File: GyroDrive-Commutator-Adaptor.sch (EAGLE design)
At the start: 26 parts, among them U1 HALL, U2 PCA9517, U3 5V, U4 2.5V, U5 INA2141U, U6 INA2141U, U7 INA2141U, X1 NORCOMP-DB25-SMD-MALE

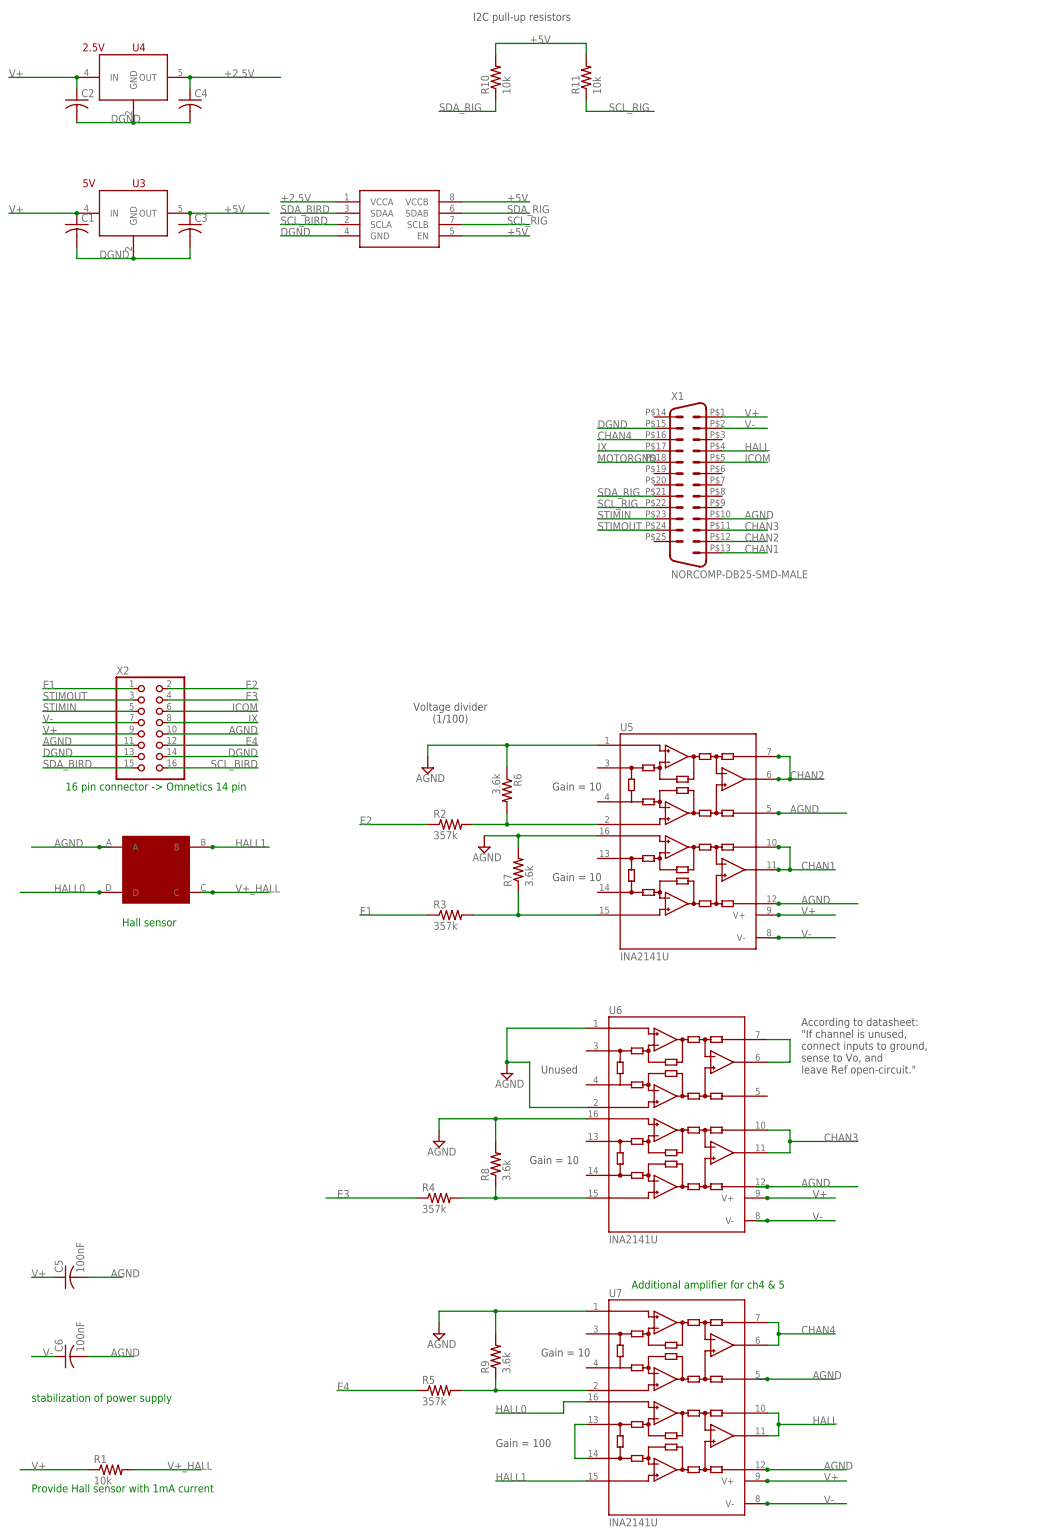
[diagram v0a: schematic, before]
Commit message: Removed instrumentation amplifiers for electrodes
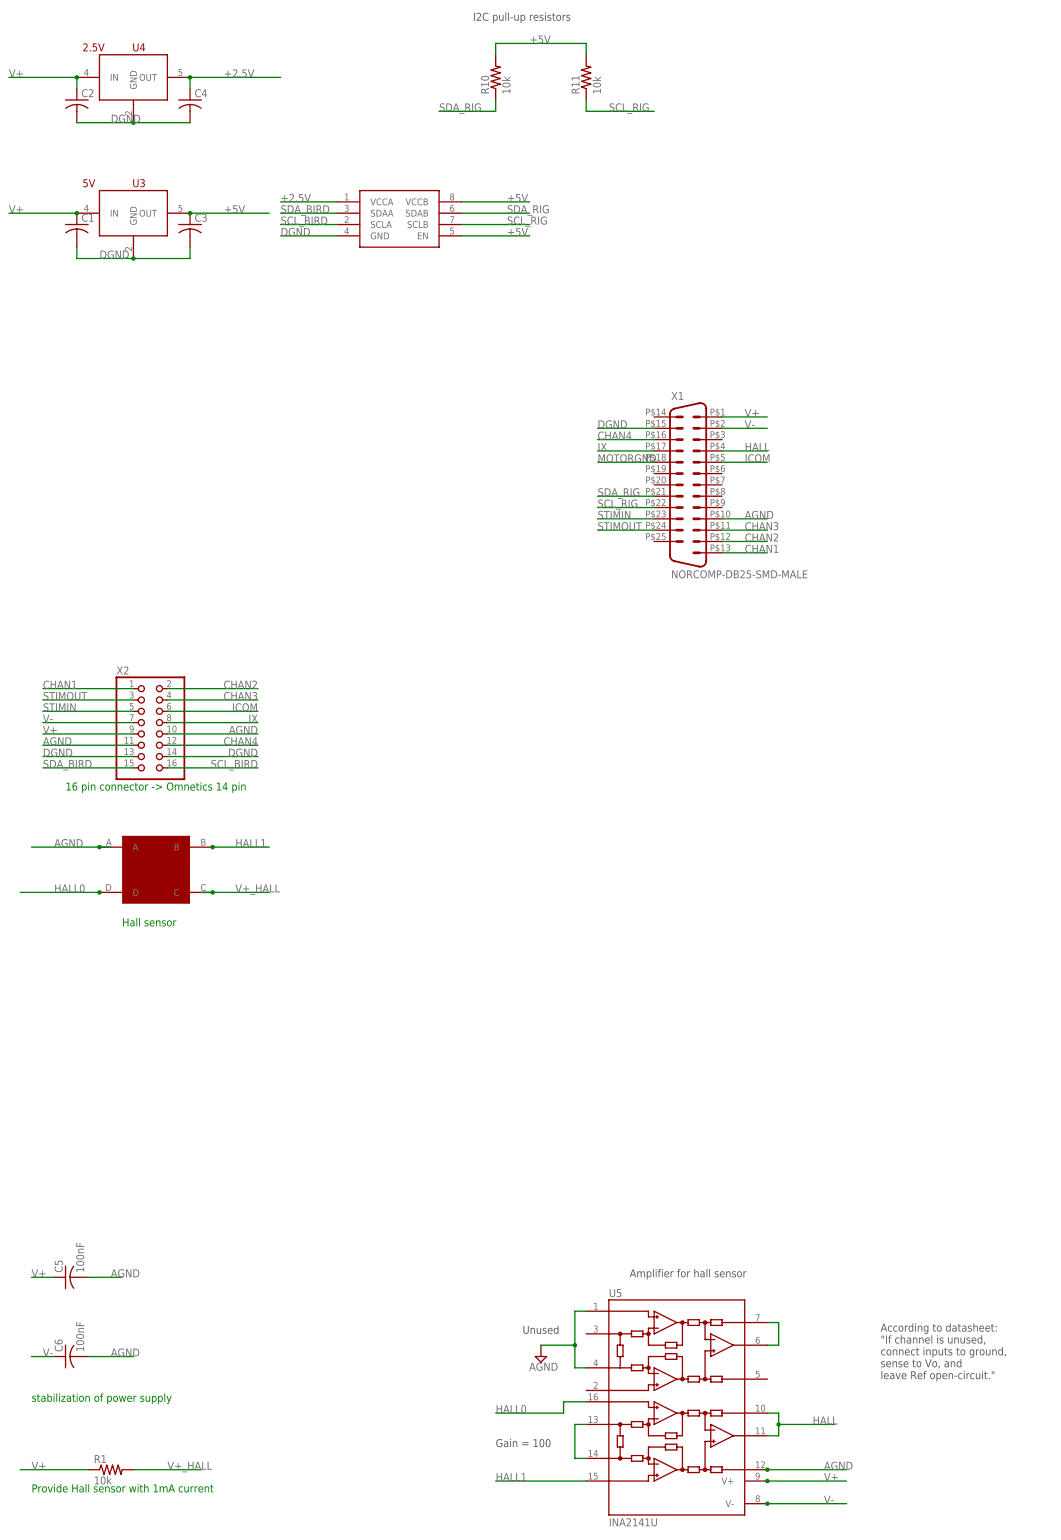
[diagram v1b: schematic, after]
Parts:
- removed R2, R3, R4, R5: 357k, resistor:R-US_R0805
- removed R6, R7, R8, R9: 3.6k, resistor:R-US_R0805
- removed U6, U7: INA2141U, burr-brown:INA2141U
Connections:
- removed net E1: R3.1, X2.1
- removed net E2: R2.1, X2.2
- removed net E3: R4.1, X2.4
- removed net E4: R5.1, X2.12
- removed net IN1: R3.2, R7.1, U5.INB+
- removed net IN2: R2.2, R6.2, U5.INA+
- removed net IN3: R4.2, R8.1, U6.INB+
- removed net IN4: R5.2, R9.1, U7.INA+
- removed net N$1: U6.SENSEA, U6.VOA
- new net UNUSED: U5.SENSEA, U5.VOA
- net AGND: now also U5.JA@1; no longer R6.1, R7.2, R8.2, R9.2, U5.INB-, U5.REFA, U6.INA+, U6.INA-, U6.INB-, U6.REFB, U7.INA-, U7.REFA, U7.REFB
- net CHAN1: now also X2.1; no longer U5.SENSEB, U5.VOB
- net CHAN2: now also X2.2; no longer U5.SENSEA, U5.VOA
- net CHAN3: now also X2.4; no longer U6.SENSEB, U6.VOB
- net CHAN4: now also X2.12; no longer U7.SENSEA, U7.VOA
- net HALL: now also U5.SENSEB, U5.VOB; no longer U7.SENSEB, U7.VOB
- net HALL0: now also U5.INB-; no longer U7.INB-
- net HALL1: now also U5.INB+; no longer U7.INB+
- net N$3: now also U5.JB, U5.JB@1; no longer U7.JB, U7.JB@1
- net V+: no longer U6.V+, U7.V+
- net V-: no longer U6.V-, U7.V-
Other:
- note added: "Amplifier for hall sensor"
- note removed: "Additional amplifier for ch4 & 5"
- note removed: "Gain = 10"
- note removed: "Voltage divider (1/100)"
- moved on the sheet: U5
